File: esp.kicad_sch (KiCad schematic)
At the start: 30 parts, among them J1 Barrel_Jack, J2 8P8C_Shielded, J21 8P8C_Shielded, J3 Barrel_Jack, J38 8P8C_Shielded, J4 Barrel_Jack, J5 Barrel_Jack, J7 Barrel_Jack_MountingPin, K1 RT314A24, P1 Conn_WallPlug_Earth, U1 ESP32-S2-WROVER, U14 PCF8574ATS, U16 L298N, U17 PCA9685PW, U18 NID30S48-24, U2 TCA9548ARGER, U3 TCA9548ARGER, U4 BME280, U5 CCS811, U6 PCF8574ATS, U7 OKI-78SR-12_1.0-W36H-C, U8 OKI-78SR-5_1.5-W36-C, U9 OKI-78SR-3.3_1.5-W36H-C

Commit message: larger file for main layout
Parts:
- removed U5: CCS811, Package_LGA:AMS_LGA-10-1EP_2.7x4mm_P0.6mm, symbol Sensor_Gas:CCS811
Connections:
- net GND: now also U14.5 (VDD), U16.8 (GND), U17.1 (A0), U17.28 (VDD), U6.5 (VDD)
- net +3.3V: now reaches U17.14 (VSS)
- net at U3.22 (A0): now also U3.23 (A1)
- net +12V: now reaches U14.15 (VSS)
- net +12V: now also U16.9 (Vss)
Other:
- moved on the sheet: BT1, BT2, F1, F2, F3, F5, J1, J2, J21, J3, J38, J4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

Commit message: main sheet barrel connector
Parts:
- removed U14, U6: PCF8574ATS, Package_SO:SSOP-20_4.4x6.5mm_P0.65mm, symbol Interface_Expansion:PCF8574ATS
- removed U17: PCA9685PW, Package_SO:TSSOP-28_4.4x9.7mm_P0.65mm, symbol Driver_LED:PCA9685PW
- added C2, C3, C4, C5: 220uF, symbol Device:C_Polarized_Small_US
- added D10, D11, D12, D13, D14, D15, D16, D17, D18, D19, D20, D21, D22, D23, D24, D25, D26, D27, D28, D29, D30, D31, D32, D33, D34, D35, D36, D37, D38, D39, D40, D9: 1N4001, Diode_THT:D_DO-41_SOD81_P10.16mm_Horizontal, symbol Diode:1N4001
- added F10, F11, F12, F13, F14, F37, F38, F9: Fuse, symbol Device:Fuse
- added F39, F40, F41, F42, F43, F45, F46, F8: U6_P2, symbol Device:Polyfuse_Small
- added J11, J12, J13, J14, J27, J39, J40, J42, J43, J44, J46, J47: Barrel_Jack, symbol Connector:Barrel_Jack
- added Q10, Q11, Q3, Q4, Q5, Q6, Q7, Q8: MOSFET-NCHANNELSMD, Logic_Level_Bidirectional:SOT23-3, symbol Logic_Level_Bidirectional-eagle-import:MOSFET-NCHANNELSMD
- added R10, R11, R12, R13, R14, R15, R16, R17, R18, R20, R21, R23, R24, R7, R8, R9: 10K, Logic_Level_Bidirectional:0603-RES, symbol Logic_Level_Bidirectional-eagle-import:RESISTOR0603-RES
- added U14, U17, U6: L298N, Package_TO_SOT_THT:TO-220-15_P2.54x2.54mm_StaggerOdd_Lead4.58mm_Vertical, symbol Driver_Motor:L298N
- added U15, U20, U5: PCF8574ATS, Package_SO:SSOP-20_4.4x6.5mm_P0.65mm, symbol Interface_Expansion:PCF8574ATS
- added U19: PCA9685PW, Package_SO:TSSOP-28_4.4x9.7mm_P0.65mm, symbol Driver_LED:PCA9685PW
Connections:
- net +12V: now also U16.4 (Vs), C2.1, C3.1, C4.1, C5.1, D11.1 (K), D13.1 (K), D15.1 (K), D17.1 (K), D19.1 (K), D21.1 (K), D23.1 (K), D25.1 (K), D27.1 (K), D29.1 (K), D31.1 (K), D33.1 (K), D35.1 (K), D37.1 (K), D39.1 (K), D9.1 (K), U14.4 (Vs), U17.4 (Vs), U6.4 (Vs); no longer U16.9 (Vss)
- net +3.3V: now also Q10.1 (G), Q11.1 (G), Q3.1 (G), Q4.1 (G), Q5.1 (G), Q6.1 (G), Q7.1 (G), Q8.1 (G), R10.1, R12.1, R16.1, R17.1, R18.1, R23.1, R24.1, R8.1, U5.15 (VSS)
- net GND: now also U16.1 (SENSE_A), C2.2, C3.2, C4.2, C5.2, D10.2 (A), D12.2 (A), D14.2 (A), D16.2 (A), D18.2 (A), D20.2 (A), D22.2 (A), D24.2 (A), D26.2 (A), D28.2 (A), D30.2 (A), D32.2 (A), D34.2 (A), D36.2 (A), D38.2 (A), D40.2 (A), J11.2, J39.2, J40.2, J42.2, J43.2, J44.2, J46.2, J47.2, U14.1 (SENSE_A), U14.8 (GND), U15.6 (A0), U17.1 (SENSE_A), U17.8 (GND), U20.6 (A0), U20.7 (A1), U5.5 (VDD), U5.7 (A1), U5.9 (A2), U6.1 (SENSE_A), U6.8 (GND)
- net at J5.1: now also F12.1
- net at J5.2: now also D23.2 (A), D24.1 (K), U6.2 (OUT1)
- net at U3.1 (SD0): now also U15.4 (SDA)
- net at U3.12 (SD5): now also U5.4 (SDA)
- net at U3.13 (SC5): now also U5.2 (SCL)
- net at U3.19 (SCL): now also U1.20 (IO17)
- net at U3.2 (SC0): now also U15.2 (SCL)
- net at U3.20 (SDA): now also U1.19 (IO16)
- net at U3.3 (SD1): now also U19.27 (SDA)
- net at U3.4 (SC1): now also U19.26 (SCL)
- net at U3.5 (SD2): now also U20.4 (SDA)
- net at U3.6 (SC2): now also U20.2 (SCL)
- net at J4.1: now also F11.1
- net at J4.2: now also D19.2 (A), D20.1 (K), U6.13 (OUT3)
- net at U16.10 (IN3): now also U20.19 (P6)
- net at U16.11 (EnB): now also U19.13 (LED7)
- net at U16.12 (IN4): now also U20.20 (P7)
- net at U16.13 (OUT3): now also D29.2 (A), D30.1 (K), J12.2
- net at U16.14 (OUT4): now also D25.2 (A), D26.1 (K), F13.2
- net at U16.2 (OUT1): now also D37.2 (A), D38.1 (K), J13.2
- net at U16.3 (OUT2): now also D33.2 (A), D34.1 (K), F14.2
- net at U16.5 (IN1): now also U20.16 (P4)
- net at U16.6 (EnA): now also U19.12 (LED6)
- net at U16.7 (IN2): now also U20.17 (P5)
- net at J1.1: now also F9.1
- net at J1.2: now also D11.2 (A), D12.1 (K), U14.13 (OUT3)
- net at J3.1: now also F10.1
- net at J3.2: now also D15.2 (A), D16.1 (K), U14.2 (OUT1)
- new net: F13.1, J12.1
- new net: F46.1, J47.1
- new net: D17.2 (A), D18.1 (K), F11.2, U6.14 (OUT4)
- new net: D13.2 (A), D14.1 (K), F10.2, U14.3 (OUT2)
- new net: F37.1, J14.1
- new net: D31.2 (A), D32.1 (K), J14.2, U17.13 (OUT3)
- new net: F43.1, J44.1
- new net: F42.1, J43.1
- new net: D10.1 (K), D9.2 (A), F9.2, U14.14 (OUT4)
- new net: F8.1, J11.1
- new net: D27.2 (A), D28.1 (K), F37.2, U17.14 (OUT4)
- new net: D39.2 (A), D40.1 (K), J27.2, U17.2 (OUT1)
- new net: F45.1, J46.1
- new net: D21.2 (A), D22.1 (K), F12.2, U6.3 (OUT2)
- new net: F41.1, J42.1
- new net: U17.6 (EnA), U19.10 (LED4)
- new net: U17.11 (EnB), U19.11 (LED5)
- new net: U14.6 (EnA), U19.6 (LED0)
- new net: U14.11 (EnB), U19.7 (LED1)
- new net: U19.8 (LED2), U6.6 (EnA)
- new net: U19.9 (LED3), U6.11 (EnB)
- new net: F39.1, J39.1
- new net: U17.5 (IN1), U20.10 (P0)
- new net: U17.7 (IN2), U20.11 (P1)
- new net: U17.10 (IN3), U20.12 (P2)
- new net: U17.12 (IN4), U20.14 (P3)
- new net: U14.5 (IN1), U15.10 (P0)
- new net: U14.7 (IN2), U15.11 (P1)
- new net: U14.10 (IN3), U15.12 (P2)
- new net: U14.12 (IN4), U15.14 (P3)
- new net: U15.16 (P4), U6.5 (IN1)
- new net: U15.17 (P5), U6.7 (IN2)
- new net: U15.19 (P6), U6.10 (IN3)
- new net: U15.20 (P7), U6.12 (IN4)
- new net: F14.1, J13.1
- new net: F40.1, J40.1
- new net: D35.2 (A), D36.1 (K), F38.2, U17.3 (OUT2)
- new net: F38.1, J27.1
- new net +5V: R11.1, R13.1, R14.1, R15.1, R20.1, R21.1, R7.1, R9.1
- new net HV4: F39.2, F40.2, F41.2, F42.2, F43.2, F45.2, F46.2, F8.2, Q10.3 (D), Q11.3 (D), Q3.3 (D), Q4.3 (D), Q5.3 (D), Q6.3 (D), Q7.3 (D), Q8.3 (D), R11.2, R13.2, R14.2, R15.2, R20.2, R21.2, R7.2, R9.2
- new net LV4: Q10.2 (S), Q11.2 (S), Q3.2 (S), Q4.2 (S), Q5.2 (S), Q6.2 (S), Q7.2 (S), Q8.2 (S), R10.2, R12.2, R16.2, R17.2, R18.2, R23.2, R24.2, R8.2, U5.10 (P0), U5.11 (P1), U5.12 (P2), U5.14 (P3), U5.16 (P4), U5.17 (P5), U5.19 (P6), U5.20 (P7)
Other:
- moved on the sheet: BT1, BT2, F1, F2, F3, F5, J2, J21, J38, J7, K1, P1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

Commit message: add some relay stuff, not complete
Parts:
- removed F41, F42, F43, F45, F46: U6_P2, symbol Device:Polyfuse_Small
- removed J42, J43, J44, J46, J47: Barrel_Jack, symbol Connector:Barrel_Jack
- removed Q10, Q11, Q6, Q7, Q8: MOSFET-NCHANNELSMD, Logic_Level_Bidirectional:SOT23-3, symbol Logic_Level_Bidirectional-eagle-import:MOSFET-NCHANNELSMD
- removed R13, R14, R15, R16, R17, R18, R20, R21, R23, R24: 10K, Logic_Level_Bidirectional:0603-RES, symbol Logic_Level_Bidirectional-eagle-import:RESISTOR0603-RES
- added C6: 1QuF/50V, symbol Device:C_Small
- added K5: RT314A24, Relay_THT:Relay_SPDT_Schrack-RT1-16A-FormC_RM5mm, symbol Relay:RT314A24
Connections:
- net +12V: now also J40.1, C6.1, K5.A2
- net GND: now also C6.2, K5.11
- net LV4: no longer U5.14 (P3), U5.16 (P4), U5.17 (P5), U5.19 (P6), U5.20 (P7)
- net at F40.1: now also K5.A1; no longer J40.1
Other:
- moved on the sheet: J40

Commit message: relay from SolderedElectronics/2-channel-relay-board-hardware-design
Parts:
- added D41, D44: blue, e-radionica.com footprinti:0402LED, symbol e-radionica.com schematics:0402LED
- added D42, D45: M4_DIODA, e-radionica.com footprinti:M4_DIODA, symbol e-radionica.com schematics:M4_DIODA
- added D43: purple, e-radionica.com footprinti:0402LED, symbol e-radionica.com schematics:0402LED
- added FD1, FD2: FIDUCIAL, e-radionica.com footprinti:FIDUCIAL_23, symbol e-radionica.com schematics:FIDUCIAL
- added H1, H2, H3, H4: HOLE_3.2mm, e-radionica.com footprinti:HOLE_3.2mm, symbol e-radionica.com schematics:HOLE_3.2mm
- added JP1, JP2, JP3: SMD-JUMPER-CONNECTED_TRACE_SLODERMASK, e-radionica.com footprinti:SMD-JUMPER-CONNECTED_TRACE_SLODERMASK, symbol e-radionica.com schematics:SMD-JUMPER-CONNECTED_TRACE_SLODERMASK
- added K11: HEADER_MALE_4X1, e-radionica.com footprinti:HEADER_MALE_4X1, symbol e-radionica.com schematics:HEADER_MALE_4X1
- added K12, K6: SRD-05VDC-SL-C, e-radionica.com footprinti:SRD_RELAY_5V, symbol e-radionica.com schematics:SRD_RELAY_5V
- added K13, K7: TERMINAL_KF235-5.0-3P, e-radionica.com footprinti:TERMINAL_KF235-5.0-3P, symbol e-radionica.com schematics:TERMINAL_KF235-5.0-3P
- added Q6, Q7: NPN, e-radionica.com footprinti:SOT-23-3, symbol e-radionica.com schematics:NPN-SOT-23-3
- added R13, R18: 100R, e-radionica.com footprinti:0603R, symbol e-radionica.com schematics:0603R
- added R14, R17, R19: 2k2, e-radionica.com footprinti:0402R, symbol e-radionica.com schematics:0402R
- added R15, R20: 330R, e-radionica.com footprinti:0603R, symbol e-radionica.com schematics:0603R
- added R16, R21: 10R, e-radionica.com footprinti:0603R, symbol e-radionica.com schematics:0603R
- added U21, U22: PC357_OPTO, e-radionica.com footprinti:PC357_OPTO, symbol e-radionica.com schematics:PC357_OPTO
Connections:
- net GND: now also D43.2 (K), K11.4, Q6.2 (E), Q7.2 (E), U21.2 (katoda), U22.2 (katoda)
- new net: D44.2 (K), R19.2
- new net: R18.1, U22.1 (anoda)
- new net: Q7.1 (B), U22.3 (emiter)
- new net: R20.1, U22.4 (kolektor)
- new net: JP1.1, R14.1
- new net: D41.2 (K), R14.2
- new net: D42.2 (K), K6.1, R16.1
- new net: D42.1 (A), JP1.2, K6.2, Q6.3 (C)
- new net: JP3.1, R19.1
- new net: D43.1 (A), R17.2
- new net: D45.1 (A), JP3.2, K12.2, Q7.3 (C)
- new net: JP2.2, R17.1
- new net: D45.2 (K), K12.1, R21.1
- new net: R13.1, U21.1 (anoda)
- new net: Q6.1 (B), U21.3 (emiter)
- new net: R15.1, U21.4 (kolektor)
- new net COM1: K6.4, K7.2
- new net COM2: K12.4, K13.2
- new net IN1: K11.2, R13.2
- new net IN2: K11.3, R18.2
- new net NC1: K6.5, K7.1
- new net NC2: K12.5, K13.1
- new net NO1: K6.3, K7.3
- new net NO2: K12.3, K13.3
- new net VCC: D41.1 (A), D44.1 (A), JP2.1, K11.1, R15.2, R16.2, R20.2, R21.2
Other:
- note added: "HEADER"
- note added: "PWR LED"
- note added: "RELAY1"
- note added: "RELAY2"

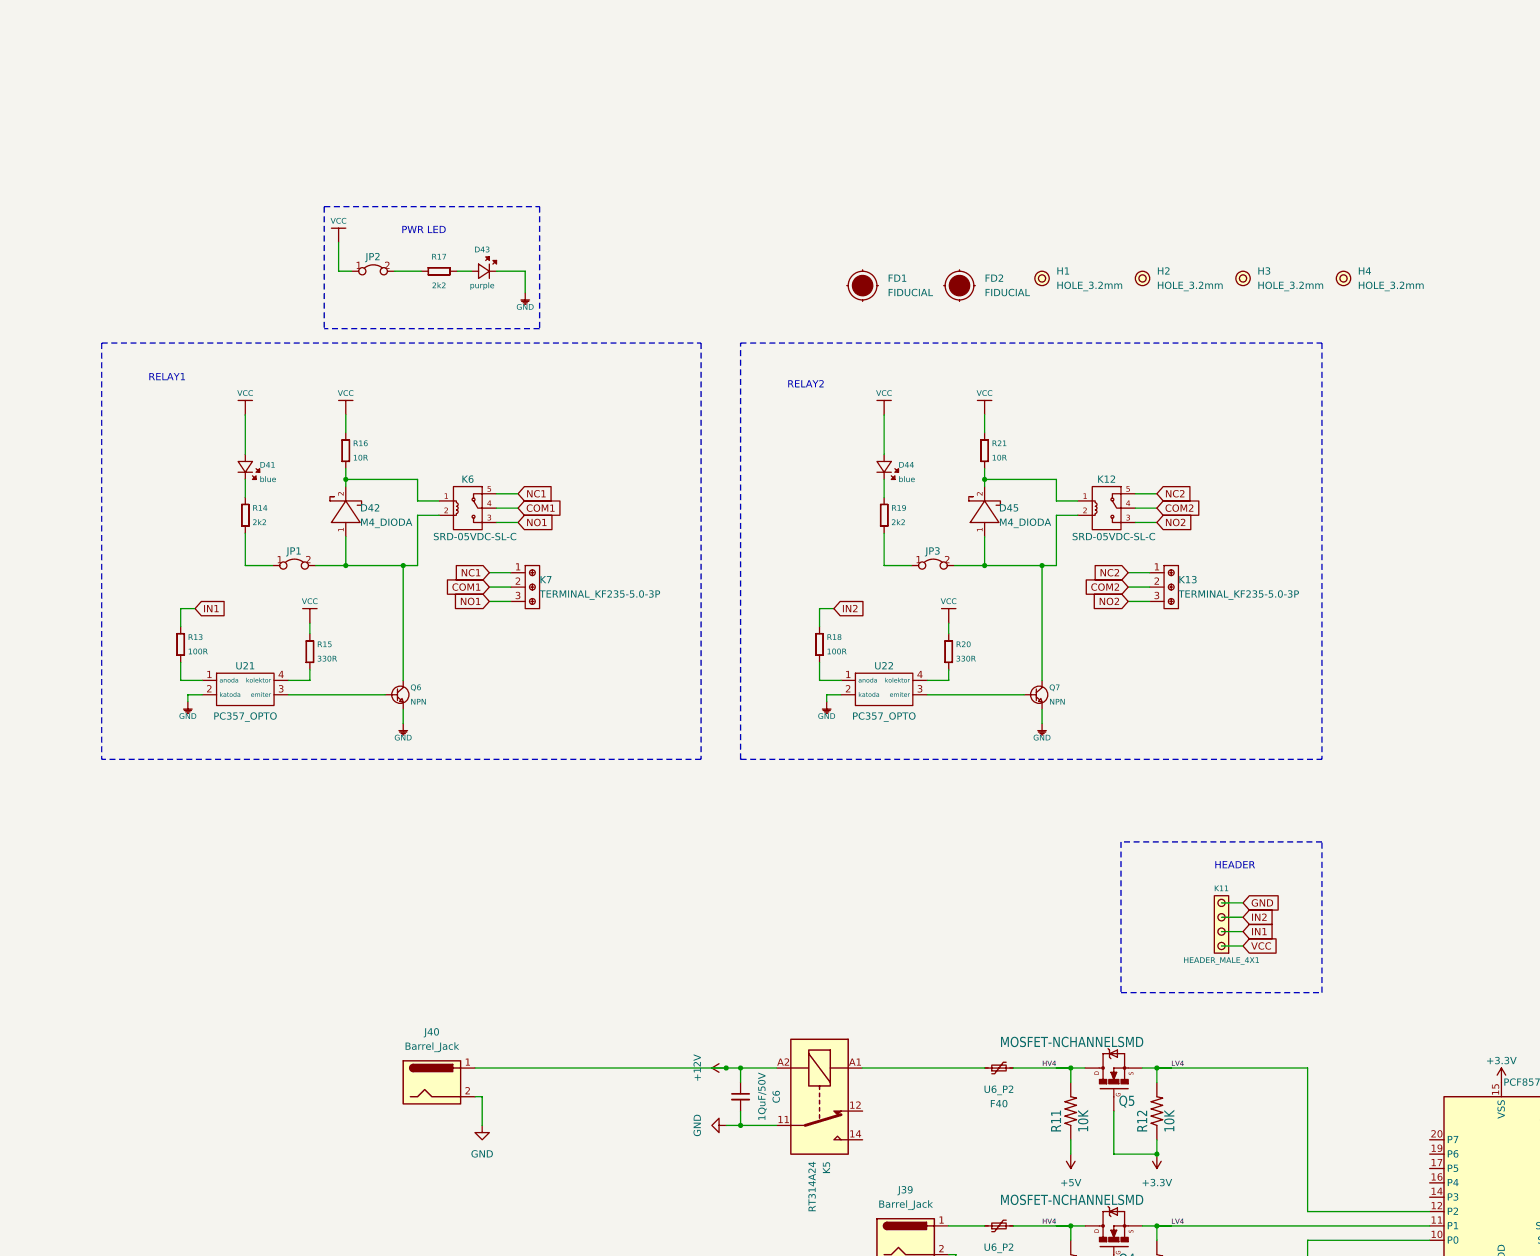
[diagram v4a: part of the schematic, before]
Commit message: relay from SolderedElectronics/2-channel-relay-board-hardware-design added clean up and connections to gpio expander todo: check to see if this works with 3.3 v or put a level shifter
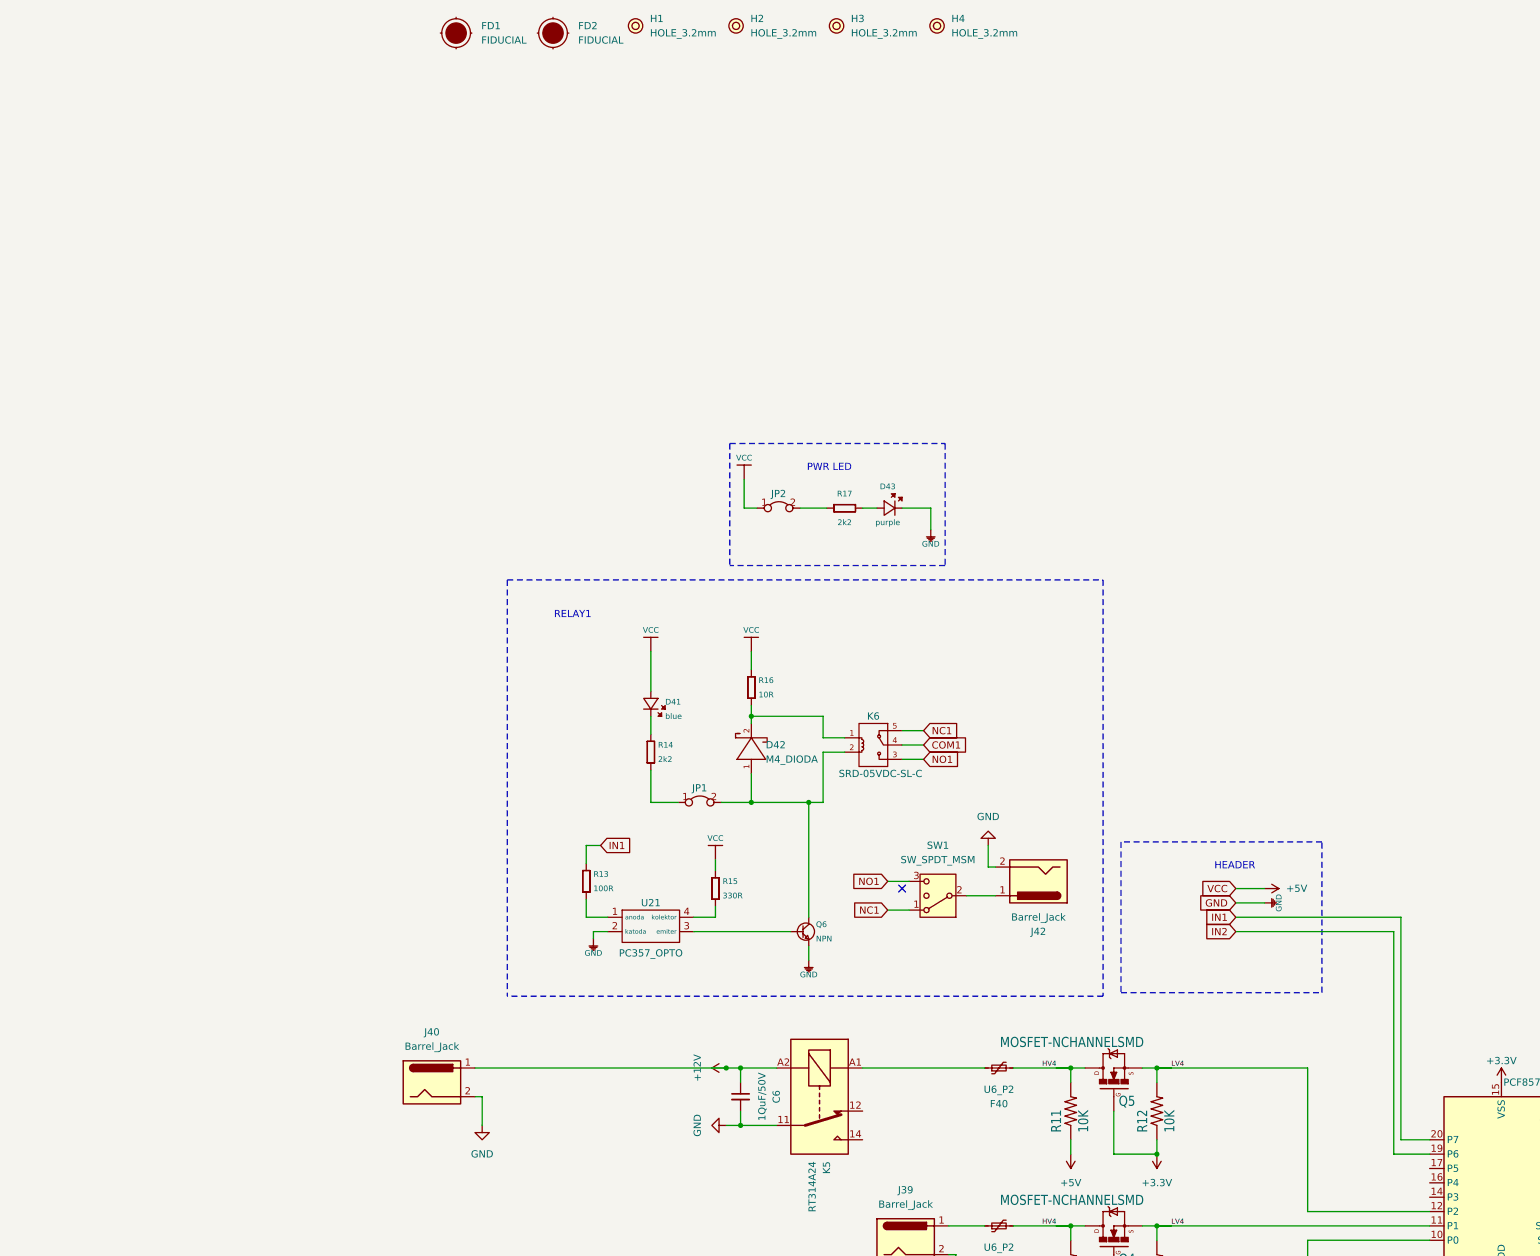
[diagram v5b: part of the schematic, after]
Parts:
- removed D44: blue, e-radionica.com footprinti:0402LED, symbol e-radionica.com schematics:0402LED
- removed D45: M4_DIODA, e-radionica.com footprinti:M4_DIODA, symbol e-radionica.com schematics:M4_DIODA
- removed JP3: SMD-JUMPER-CONNECTED_TRACE_SLODERMASK, e-radionica.com footprinti:SMD-JUMPER-CONNECTED_TRACE_SLODERMASK, symbol e-radionica.com schematics:SMD-JUMPER-CONNECTED_TRACE_SLODERMASK
- removed K11: HEADER_MALE_4X1, e-radionica.com footprinti:HEADER_MALE_4X1, symbol e-radionica.com schematics:HEADER_MALE_4X1
- removed K12: SRD-05VDC-SL-C, e-radionica.com footprinti:SRD_RELAY_5V, symbol e-radionica.com schematics:SRD_RELAY_5V
- removed K13, K7: TERMINAL_KF235-5.0-3P, e-radionica.com footprinti:TERMINAL_KF235-5.0-3P, symbol e-radionica.com schematics:TERMINAL_KF235-5.0-3P
- removed Q7: NPN, e-radionica.com footprinti:SOT-23-3, symbol e-radionica.com schematics:NPN-SOT-23-3
- removed R18: 100R, e-radionica.com footprinti:0603R, symbol e-radionica.com schematics:0603R
- removed R19: 2k2, e-radionica.com footprinti:0402R, symbol e-radionica.com schematics:0402R
- removed R20: 330R, e-radionica.com footprinti:0603R, symbol e-radionica.com schematics:0603R
- removed R21: 10R, e-radionica.com footprinti:0603R, symbol e-radionica.com schematics:0603R
- removed U22: PC357_OPTO, e-radionica.com footprinti:PC357_OPTO, symbol e-radionica.com schematics:PC357_OPTO
- added J42: Barrel_Jack, symbol Connector:Barrel_Jack
- added SW1: SW_SPDT_MSM, symbol Switch:SW_SPDT_MSM
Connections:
- net VCC is gone; now on net +5V: D41.1 (A), JP2.1, R15.2, R16.2
- net GND: now also J42.2
- net IN1: now also U5.20 (P7)
- net IN2: now also U5.19 (P6)
- net NC1: now also SW1.1
- net NO1: now also SW1.3 (4)
- new net: J42.1, SW1.2 (3)
- no-connect marks 0 -> 1
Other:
- note removed: "RELAY2"
- moved on the sheet: D41, D42, D43, JP1, JP2, K6, Q6, R13, R14, R15, R16, R17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

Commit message: evening cleanup
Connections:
- net +12V: no longer U14.4 (Vs), U16.4 (Vs), U17.4 (Vs), U6.4 (Vs)
- net +5V: now also U14.9 (Vss), U16.9 (Vss), U17.9 (Vss), U6.9 (Vss)
- net GND: now also U14.4 (Vs), U16.4 (Vs), U17.4 (Vs), U5.6 (A0), U6.4 (Vs); no longer U5.7 (A1)

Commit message: global labels for simple viewing
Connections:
- net +5V: now also U15.5 (VDD), U19.28 (VDD), U20.5 (VDD)
- net GND: now also U15.15 (VSS), U19.1 (A0), U19.14 (VSS), U20.15 (VSS)
- net IN1: now also U5.10 (P0); no longer U5.20 (P7)
- net IN2: now also U5.11 (P1); no longer U5.19 (P6)
- net at U3.12 (SD5): no longer U5.4 (SDA)
- net at U3.13 (SC5): no longer U5.2 (SCL)
- net TCA_2_SD7: now reaches U3.16 (SD7)
- net TCA_2_SD7: now also U5.4 (SDA)
- net TCA_2_SC7: now reaches U3.17 (SC7)
- net TCA_2_SC7: now also U5.2 (SCL)
- net PCA_0_LED_4: now reaches U17.6 (EnA), U19.10 (LED4)
- net PCA_0_LED_5: now reaches U17.11 (EnB), U19.11 (LED5)
- net PCA_0_LED_6: now reaches U16.6 (EnA), U19.12 (LED6)
- net PCA_0_LED_7: now reaches U16.11 (EnB), U19.13 (LED7)
- net PCA_0_LED_8: now reaches U19.15 (LED8)
- net PCA_0_LED_9: now reaches U19.16 (LED9)
- net PCA_0_LED_10: now reaches U19.17 (LED10)
- net PCA_0_LED_11: now reaches U19.18 (LED11)
- net PCA_0_LED_12: now reaches U19.19 (LED12)
- net PCA_0_LED_13: now reaches U19.20 (LED13)
- net PCA_0_LED_14: now reaches U19.21 (LED14)
- net PCA_0_LED_15: now reaches U19.22 (LED15)
- net PCA_0_LED_0: now reaches U14.6 (EnA), U19.6 (LED0)
- net PCA_0_LED_1: now reaches U14.11 (EnB), U19.7 (LED1)
- net PCA_0_LED_2: now reaches U19.8 (LED2), U6.6 (EnA)
- net PCA_0_LED_3: now reaches U19.9 (LED3), U6.11 (EnB)
- net PCF_20_GPIO_0: now reaches U17.5 (IN1), U20.10 (P0)
- net PCF_20_GPIO_1: now reaches U17.7 (IN2), U20.11 (P1)
- net PCF_20_GPIO_2: now reaches U17.10 (IN3), U20.12 (P2)
- net PCF_20_GPIO_3: now reaches U17.12 (IN4), U20.14 (P3)
- net PCF_20_GPIO_4: now reaches U16.5 (IN1), U20.16 (P4)
- net PCF_20_GPIO_5: now reaches U16.7 (IN2), U20.17 (P5)
- net PCF_20_GPIO_6: now reaches U16.10 (IN3), U20.19 (P6)
- net PCF_20_GPIO_7: now reaches U16.12 (IN4), U20.20 (P7)
- net PCF_0_GPIO_0: now reaches U14.5 (IN1), U15.10 (P0)
- net PCF_0_GPIO_1: now reaches U14.7 (IN2), U15.11 (P1)
- net PCF_0_GPIO_2: now reaches U14.10 (IN3), U15.12 (P2)
- net PCF_0_GPIO_3: now reaches U14.12 (IN4), U15.14 (P3)
- net PCF_0_GPIO_4: now reaches U15.16 (P4), U6.5 (IN1)
- net PCF_0_GPIO_5: now reaches U15.17 (P5), U6.7 (IN2)
- net PCF_0_GPIO_6: now reaches U15.19 (P6), U6.10 (IN3)
- net PCF_0_GPIO_7: now reaches U15.20 (P7), U6.12 (IN4)
- net IN4: now reaches U5.14 (P3)
- net IN5: now reaches U5.16 (P4)
- net IN6: now reaches U5.17 (P5)
- net LV4 renamed PCF_1_GPIO_0
- net PCF_1_GPIO_0: no longer U5.10 (P0), U5.11 (P1), U5.12 (P2)
- new net IN3: U5.12 (P2)
- new net IN7: U5.19 (P6), U5.20 (P7)
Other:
- moved on the sheet: D41, D42, D43, FD1, FD2, H1, H2, H3, H4, J42, JP1, JP2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
